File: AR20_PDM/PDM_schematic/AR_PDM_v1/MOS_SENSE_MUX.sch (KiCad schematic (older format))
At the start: 14 parts, among them Q10 N_FET, Q11 N_FET, Q12 N_FET, Q13 N_FET, Q14 N_FET, Q15 N_FET, Q9 N_FET

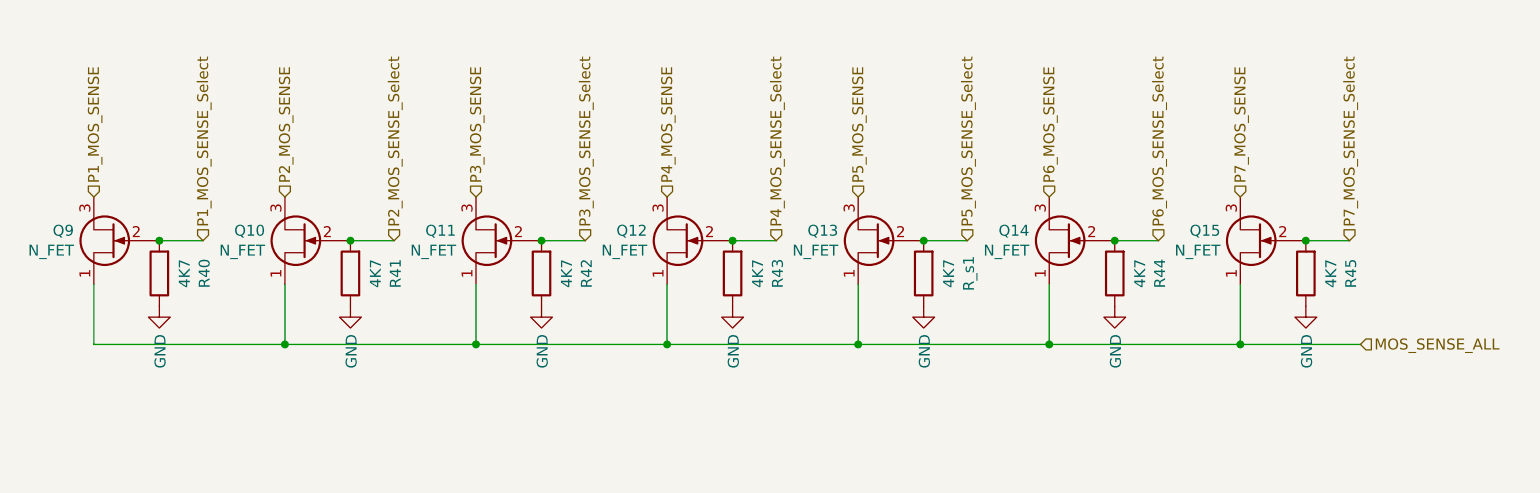
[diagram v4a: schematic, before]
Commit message: Fixed wrong resistors, mos sense. Gerber files updated
- removed all R_is_protection resistors on each mosfet line
- added one R_is_protection resistors to mos_sense_all
ps, mux N-fets, does not need overvoltage protection. 60 volt tolerant.
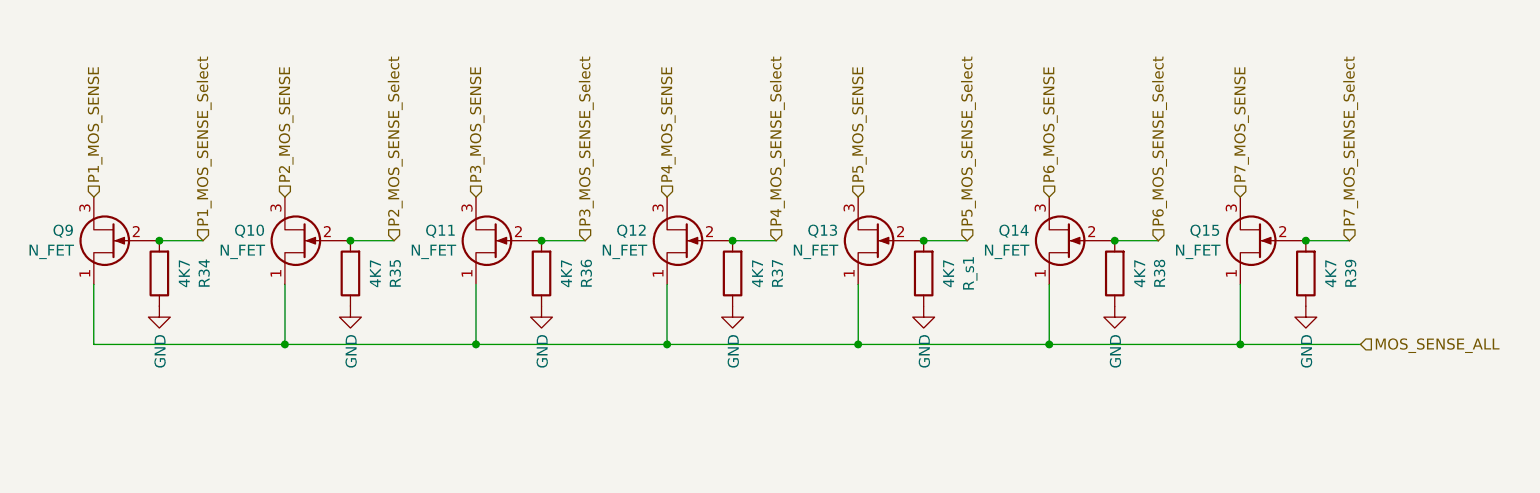
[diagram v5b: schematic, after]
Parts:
- renumbered R40 to R34, R41 to R35, R42 to R36, R43 to R37, R44 to R38, R45 to R39
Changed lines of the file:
@@
 AR Path="/5DA89415/5E25DB2C" Ref="R?"  Part="1"
 AR Path="/5DA8920B/5E25DB2C" Ref="R?"  Part="1"
-AR Path="/5E2546F2/5E25DB2C" Ref="R40"  Part="1"
-F 0 "R40" V 1093 2175 50  0000 C CNN
+AR Path="/5E2546F2/5E25DB2C" Ref="R34"  Part="1"
+F 0 "R34" V 1093 2175 50  0000 C CNN
 F 1 "4K7" V 1184 2175 50  0000 C CNN
 F 2 "Resistor_SMD:R_0603_1608Metric" V 1230 2175 50  0001 C CNN
@@
 AR Path="/5DA89415/5E26327C" Ref="R?"  Part="1"
 AR Path="/5DA8920B/5E26327C" Ref="R?"  Part="1"
-AR Path="/5E2546F2/5E26327C" Ref="R41"  Part="1"
-F 0 "R41" V 1968 2175 50  0000 C CNN
+AR Path="/5E2546F2/5E26327C" Ref="R35"  Part="1"
+F 0 "R35" V 1968 2175 50  0000 C CNN
 F 1 "4K7" V 2059 2175 50  0000 C CNN
 F 2 "Resistor_SMD:R_0603_1608Metric" V 2105 2175 50  0001 C CNN
@@
 AR Path="/5DA89415/5E263C2D" Ref="R?"  Part="1"
 AR Path="/5DA8920B/5E263C2D" Ref="R?"  Part="1"
-AR Path="/5E2546F2/5E263C2D" Ref="R42"  Part="1"
-F 0 "R42" V 2843 2175 50  0000 C CNN
+AR Path="/5E2546F2/5E263C2D" Ref="R36"  Part="1"
+F 0 "R36" V 2843 2175 50  0000 C CNN
 F 1 "4K7" V 2934 2175 50  0000 C CNN
 F 2 "Resistor_SMD:R_0603_1608Metric" V 2980 2175 50  0001 C CNN
@@
 AR Path="/5DA89415/5E264DB3" Ref="R?"  Part="1"
 AR Path="/5DA8920B/5E264DB3" Ref="R?"  Part="1"
-AR Path="/5E2546F2/5E264DB3" Ref="R43"  Part="1"
-F 0 "R43" V 3718 2175 50  0000 C CNN
+AR Path="/5E2546F2/5E264DB3" Ref="R37"  Part="1"
+F 0 "R37" V 3718 2175 50  0000 C CNN
 F 1 "4K7" V 3809 2175 50  0000 C CNN
 F 2 "Resistor_SMD:R_0603_1608Metric" V 3855 2175 50  0001 C CNN
@@
 AR Path="/5DA89415/5E26A054" Ref="R?"  Part="1"
 AR Path="/5DA8920B/5E26A054" Ref="R?"  Part="1"
-AR Path="/5E2546F2/5E26A054" Ref="R44"  Part="1"
-F 0 "R44" V 5468 2175 50  0000 C CNN
+AR Path="/5E2546F2/5E26A054" Ref="R38"  Part="1"
+F 0 "R38" V 5468 2175 50  0000 C CNN
 F 1 "4K7" V 5559 2175 50  0000 C CNN
 F 2 "Resistor_SMD:R_0603_1608Metric" V 5605 2175 50  0001 C CNN
@@
 AR Path="/5DA89415/5E26B543" Ref="R?"  Part="1"
 AR Path="/5DA8920B/5E26B543" Ref="R?"  Part="1"
-AR Path="/5E2546F2/5E26B543" Ref="R45"  Part="1"
-F 0 "R45" V 6343 2175 50  0000 C CNN
+AR Path="/5E2546F2/5E26B543" Ref="R39"  Part="1"
+F 0 "R39" V 6343 2175 50  0000 C CNN
 F 1 "4K7" V 6434 2175 50  0000 C CNN
 F 2 "Resistor_SMD:R_0603_1608Metric" V 6480 2175 50  0001 C CNN

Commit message: Major redesign. schematics completed, PCB work in progress
-TODO : A proper changelog file. Where all changes will apear 
- Redesigned schematics to accommodate errors in the improvement list
- More detail in ALPHA improvement list
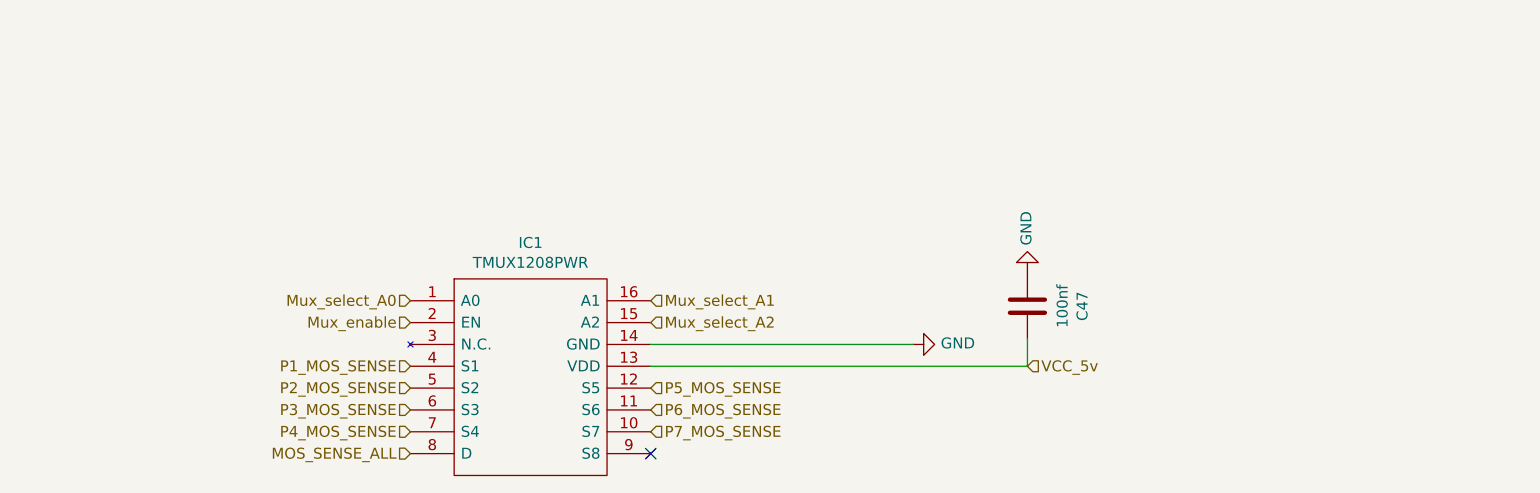
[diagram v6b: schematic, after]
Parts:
- removed Q10, Q11, Q12, Q13, Q14, Q15, Q9: N_FET, Package_TO_SOT_SMD:SOT-23, symbol Device:Q_NJFET_DGS
- removed R34, R35, R36, R37, R38, R39, R_s1: 4K7, Resistor_SMD:R_0603_1608Metric, symbol AR20_PDM_v1-rescue:R-Device
- added C47: 100nf, Capacitor_SMD:C_0603_1608Metric, symbol AR20_PDM_v1-rescue:C-Device
- added IC1: TMUX1208PWR, AR_PDM_v1:TMUX1208PWR, symbol AR20_PDM_v1-rescue:TMUX1208PWR
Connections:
- net GND: now also C47.2, IC1.14 (GND)
- net MOS_SENSE_ALL: now also IC1.8 (D)
- net P1_MOS_SENSE: now also IC1.4 (S1)
- net P2_MOS_SENSE: now also IC1.5 (S2)
- net P3_MOS_SENSE: now also IC1.6 (S3)
- net P4_MOS_SENSE: now also IC1.7 (S4)
- net P5_MOS_SENSE: now also IC1.12 (S5)
- net P6_MOS_SENSE: now also IC1.11 (S6)
- net P7_MOS_SENSE: now also IC1.10 (S7)
- new net Mux_enable: IC1.2 (EN)
- new net Mux_select_A0: IC1.1 (A0)
- new net Mux_select_A1: IC1.16 (A1)
- new net Mux_select_A2: IC1.15 (A2)
- new net VCC_5v: C47.1, IC1.13 (VDD)
- no-connect marks 0 -> 1

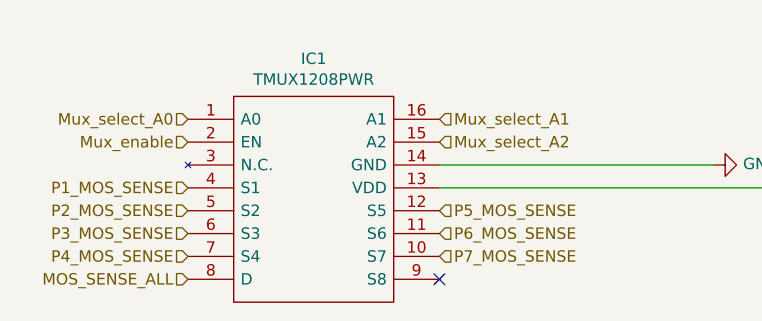
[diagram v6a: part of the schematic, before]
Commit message: All components in place - PCB work in progress
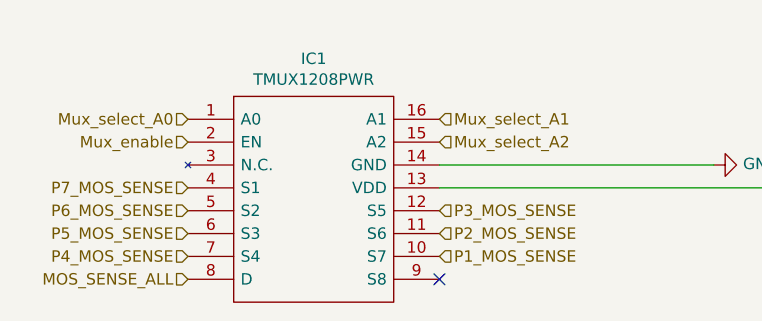
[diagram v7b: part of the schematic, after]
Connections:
- net P1_MOS_SENSE: now also IC1.10 (S7); no longer IC1.4 (S1)
- net P2_MOS_SENSE: now also IC1.11 (S6); no longer IC1.5 (S2)
- net P3_MOS_SENSE: now also IC1.12 (S5); no longer IC1.6 (S3)
- net P5_MOS_SENSE: now also IC1.6 (S3); no longer IC1.12 (S5)
- net P6_MOS_SENSE: now also IC1.5 (S2); no longer IC1.11 (S6)
- net P7_MOS_SENSE: now also IC1.4 (S1); no longer IC1.10 (S7)
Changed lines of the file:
@@
 Comment4 ""
 $EndDescr
-Text HLabel 2450 2600 0    50   Input ~ 0
-P1_MOS_SENSE
+Text HLabel 2450 2800 0    50   Input ~ 0
+P5_MOS_SENSE
 Text HLabel 2450 2700 0    50   Input ~ 0
-P2_MOS_SENSE
-Text HLabel 2450 2800 0    50   Input ~ 0
-P3_MOS_SENSE
-Text HLabel 2450 2900 0    50   Input ~ 0
-P4_MOS_SENSE
-Text HLabel 3550 2700 2    50   Input ~ 0
-P5_MOS_SENSE
-Text HLabel 3550 2800 2    50   Input ~ 0
 P6_MOS_SENSE
 Text HLabel 2450 3000 0    50   Input ~ 0
 MOS_SENSE_ALL
-Text HLabel 3550 2900 2    50   Input ~ 0
+Text HLabel 2450 2600 0    50   Input ~ 0
 P7_MOS_SENSE
 Text HLabel 3550 2400 2    50   Input ~ 0
@@
 Text HLabel 2450 2400 0    50   Input ~ 0
 Mux_enable
+Text HLabel 2450 2900 0    50   Input ~ 0
+P4_MOS_SENSE
+Text HLabel 3550 2900 2    50   Input ~ 0
+P1_MOS_SENSE
+Text HLabel 3550 2800 2    50   Input ~ 0
+P2_MOS_SENSE
+Text HLabel 3550 2700 2    50   Input ~ 0
+P3_MOS_SENSE
 $EndSCHEMATC
